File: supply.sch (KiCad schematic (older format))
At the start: 84 parts, among them IC1 TPS54561, IC2 NCP380HMUAJAATBG, J3 DC_SOCKET, Q1 BC817W, U10 REF3012AIDBZT, U4 TPS65296, U5 TPS62823DLCT

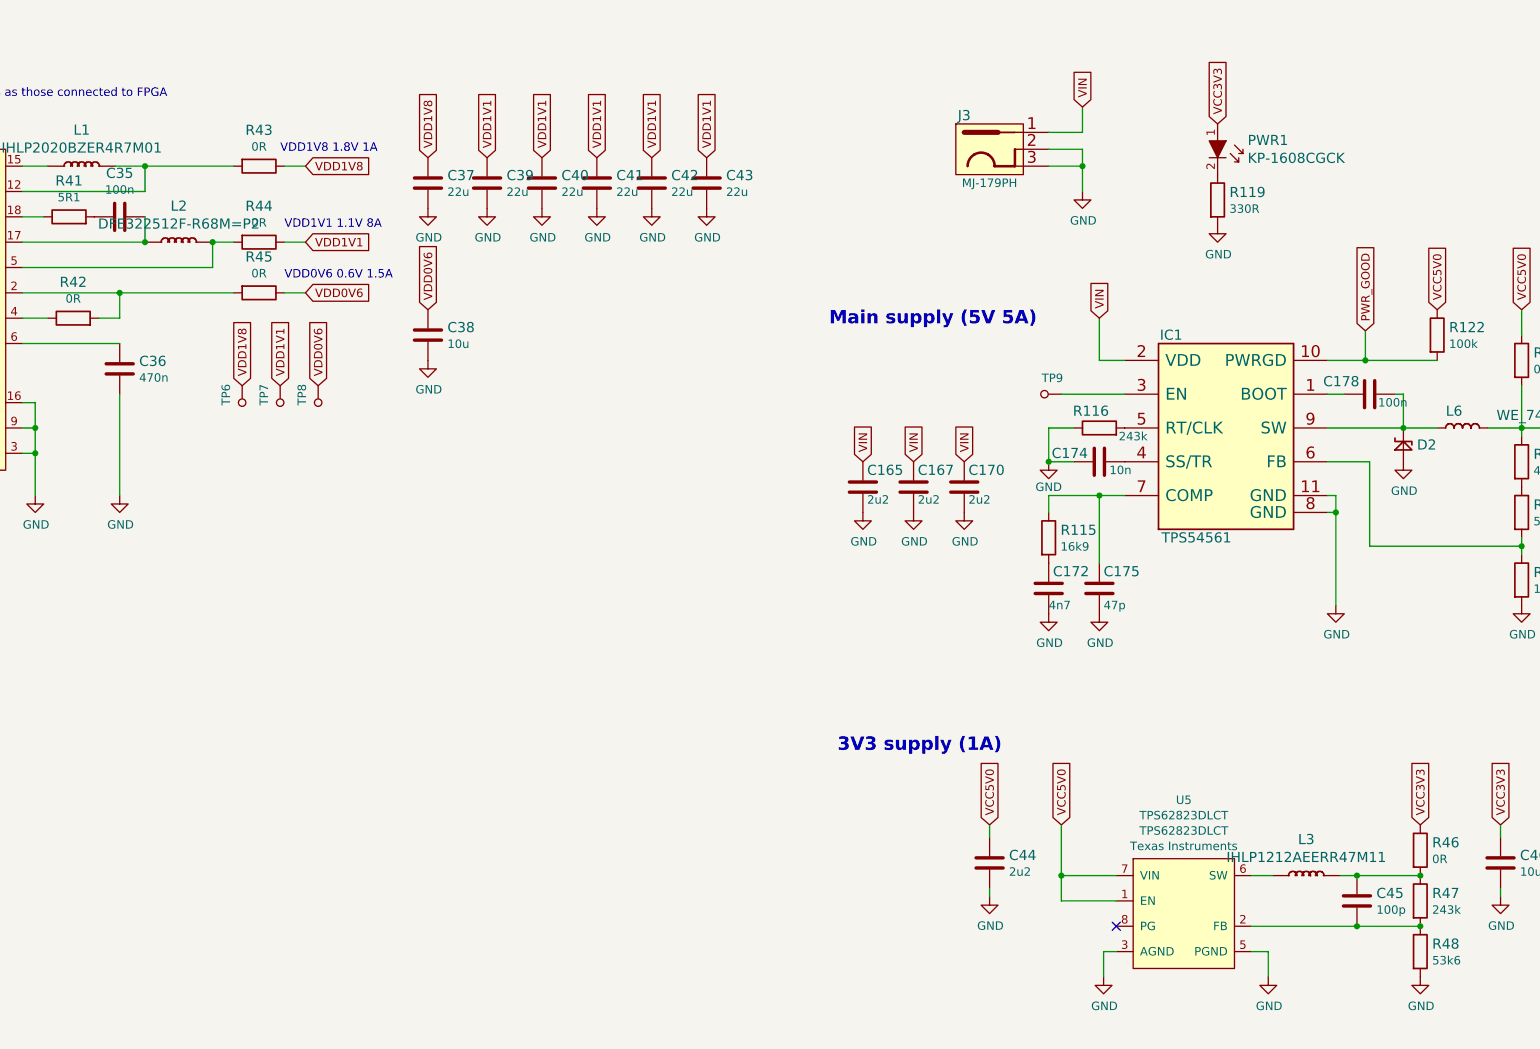
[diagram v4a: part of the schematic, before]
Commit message: Add voltage level selector
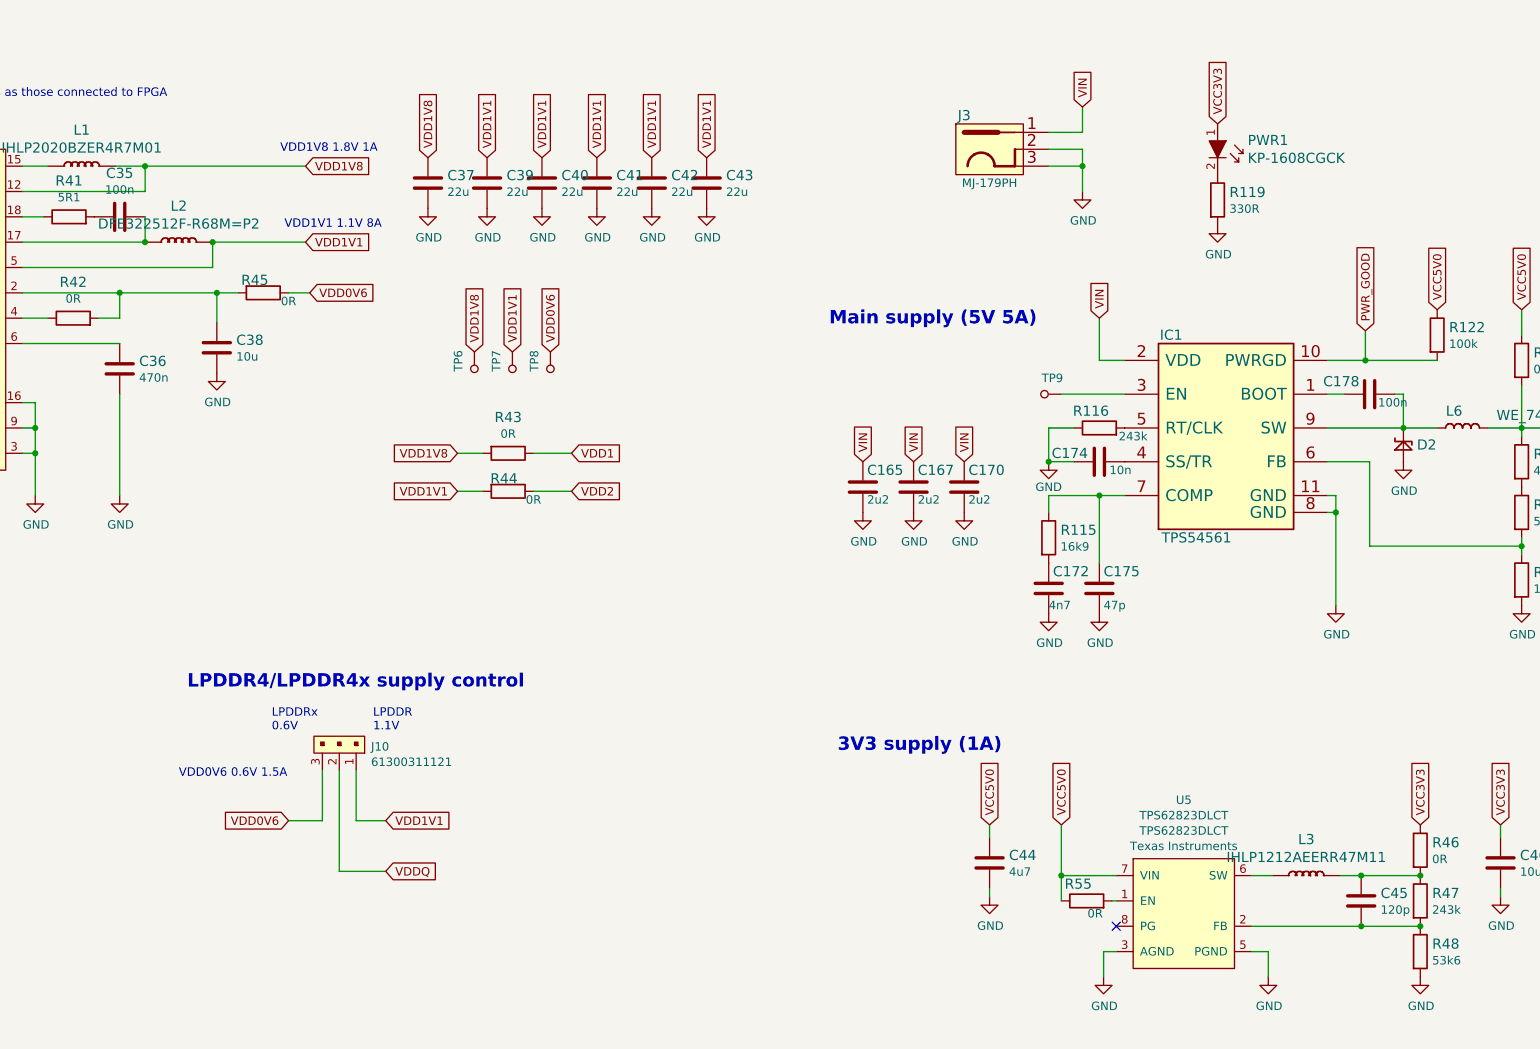
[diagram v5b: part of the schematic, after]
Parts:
- removed C44: C_2u2_0402, lpddr4-test-board-footprints:0402-cap, symbol lpddr4-test-board:C_2u2_0402
- removed C45: C_100p_0402, lpddr4-test-board-footprints:0402-cap, symbol lpddr4-test-board:C_100p_0402
- added C44: C_4u7_0603, antmicro-footprints:0603-cap, symbol antmicroCapacitors0603:C_4u7_0603
- added C45: C_120p_0603, antmicro-footprints:0603-cap, symbol antmicroCapacitors0603:C_120p_0603
- added J10: 61300311121, antmicro-footprints:PinHeader_1x3_P2.54_Drill1.1mm, symbol antmicroRectangularConnectorsHeadersMalePins:61300311121
- added R55: R_0R_0402, antmicro-footprints:0402-res, symbol antmicroResistors0402:R_0R_0402
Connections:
- net GND: now also C44.2
- net VCC5V0: now also C44.1, R55.1; no longer U5.1 (EN)
- net VDD0V6: now also J10.3; no longer C38.1
- net VDD1V1: now also L2.2 (P), R44.2, U4.5 (VDD2SNS), J10.1; no longer R44.1
- net VDD1V8: now also L1.2 (P), R43.2, U4.12 (VDD1SNS); no longer R43.1
- net at R42.2, R45.2, U4.2 (VDDQ): now also C38.1
- net at R47.2, R48.1, U5.2 (FB): now also C45.2
- net at L3.2 (P), R46.2, R47.1: now also C45.1
- new net: R55.2, U5.1 (EN)
- new net VDD1: R43.1
- new net VDD2: R44.1
- new net VDDQ: J10.2
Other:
- note added: "LPDDR4/LPDDR4x supply control"
- note added: "LPDDR\n1.1V"
- note added: "LPDDRx\n0.6V\n"
- moved on the sheet: C38, R43, R44, TP6, TP7, TP8

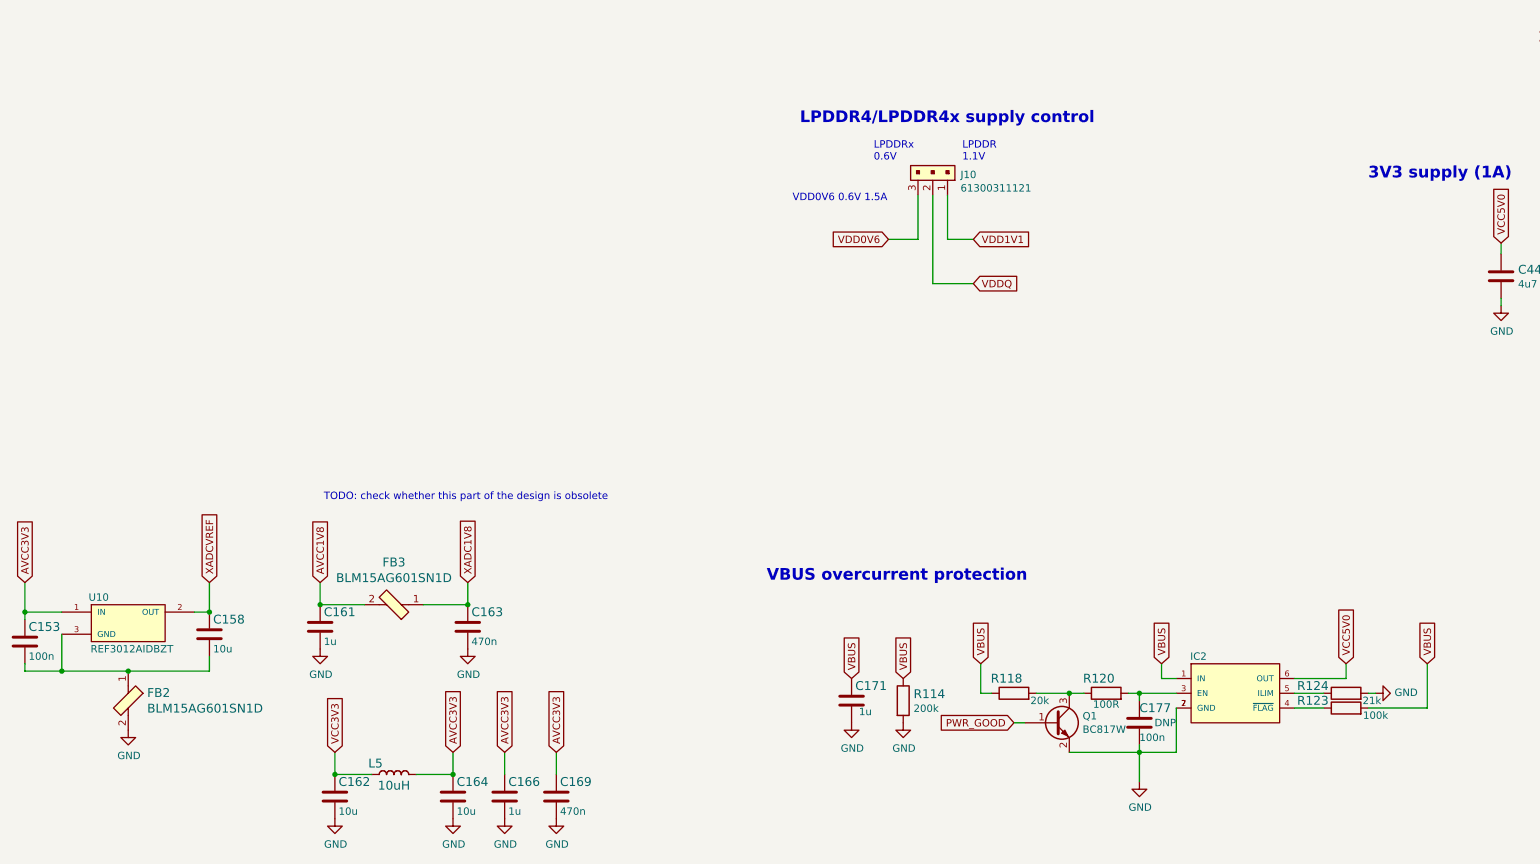
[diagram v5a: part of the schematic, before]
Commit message: Remove XADC circuit
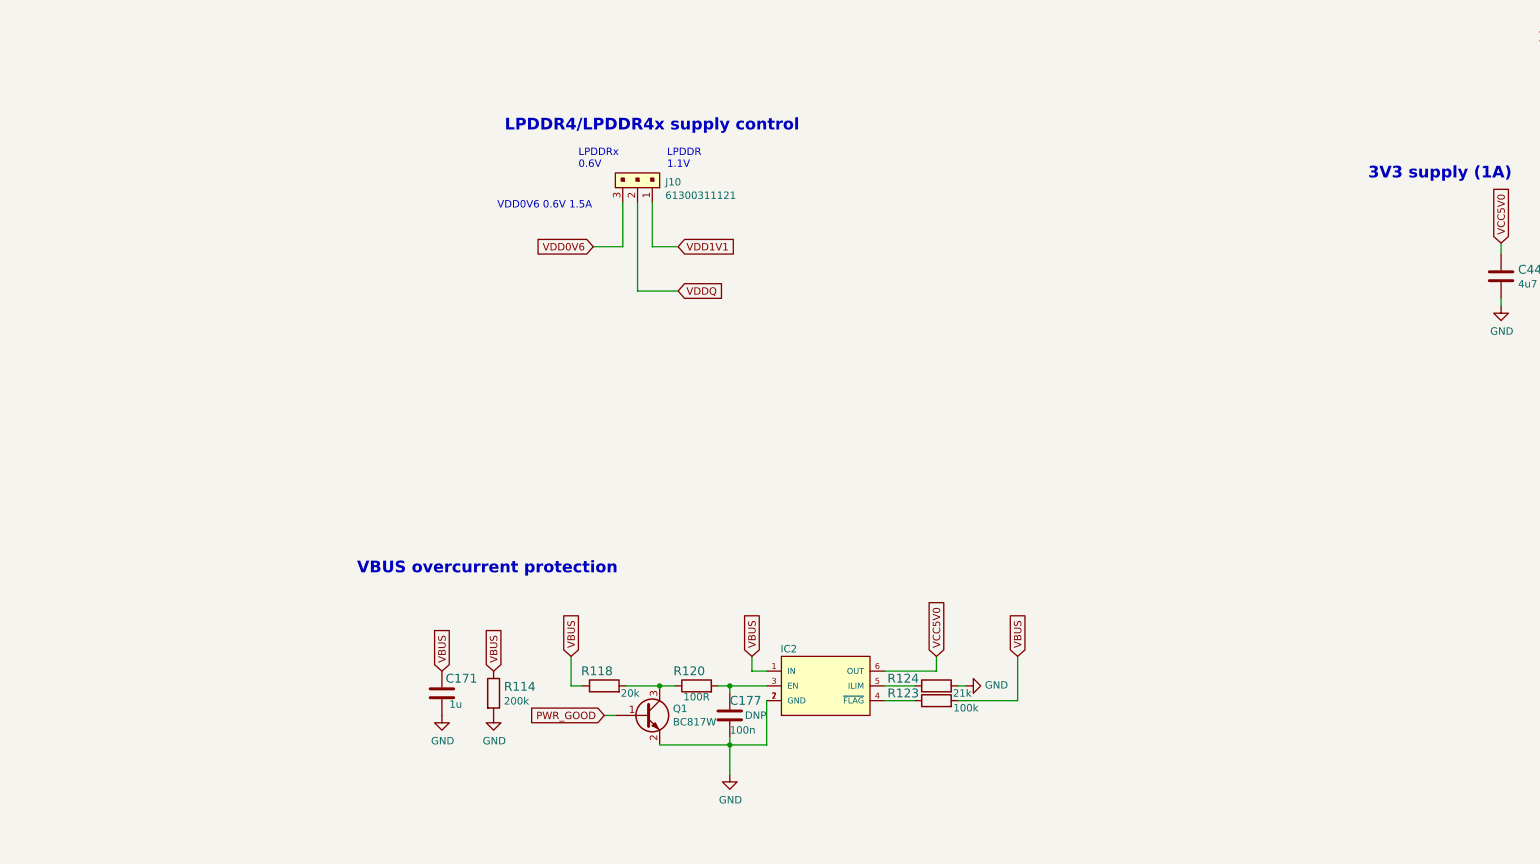
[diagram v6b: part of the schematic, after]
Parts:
- removed C153: C_100n_0402_6V3, lpddr4-test-board-footprints:0402-cap, symbol lpddr4-test-board:C_100n_0402_6V3
- removed C158, C162, C164: C_10u_0402, lpddr4-test-board-footprints:0402-cap, symbol lpddr4-test-board:C_10u_0402
- removed C161, C166: C_1u_0402, lpddr4-test-board-footprints:0402-cap, symbol lpddr4-test-board:C_1u_0402
- removed C163, C169: C_470n_0402, lpddr4-test-board-footprints:0402-cap, symbol lpddr4-test-board:C_470n_0402
- removed FB2, FB3: BLM15AG601SN1D, lpddr4-test-board-footprints:0402-res, symbol lpddr4-test-board:BLM15AG601SN1D
- removed L5: 10uH, lpddr4-test-board-footprints:0805-res, symbol lpddr4-test-board:10uH
- removed U10: REF3012AIDBZT, lpddr4-test-board-footprints:SOT-23-3, symbol lpddr4-test-board:REF3012AIDBZT
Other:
- note removed: "TODO: check whether this part of the design is obsolete"
- moved on the sheet: C171, C177, IC2, J10, Q1, R114, R118, R120, R123, R124
